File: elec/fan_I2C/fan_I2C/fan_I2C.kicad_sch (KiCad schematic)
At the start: 22 parts, among them J101 DB25_Female_MountingHoles, J102 DB9_Female_MountingHoles, J103 Screw_Terminal_01x02, J104 Conn_01x04, J105 Conn_01x05, J106 Conn_01x04, J107 Conn_01x07, J108 Screw_Terminal_01x02, J109 Conn_02x12_Odd_Even, SW101 SW_DIP_x08

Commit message: Add 3D model to Arduino.
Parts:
- XA101: footprint arduino-library:Arduino_Due_Shield -> PubInv_PCB:Arduino_Due_Shield
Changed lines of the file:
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@@
       (effects (font (size 1.524 1.524)))
     )
-    (property "Footprint" "arduino-library:Arduino_Due_Shield" (id 2) (at 194.31 166.37 0)
+    (property "Footprint" "PubInv_PCB:Arduino_Due_Shield" (id 2) (at 194.31 166.37 0)
       (effects (font (size 1.524 1.524)) hide)
     )
@@
     )
     (path "/53a9b8e5-86db-48fa-b451-066c5e8062db"
-      (reference "XA101") (unit 1) (value "Arduino_Due_Shield") (footprint "arduino-library:Arduino_Due_Shield")
-    )
-  )
+      (reference "XA101") (unit 1) (value "Arduino_Due_Shield") (footprint "PubInv_PCB:Arduino_Due_Shield")
+    )
+  )

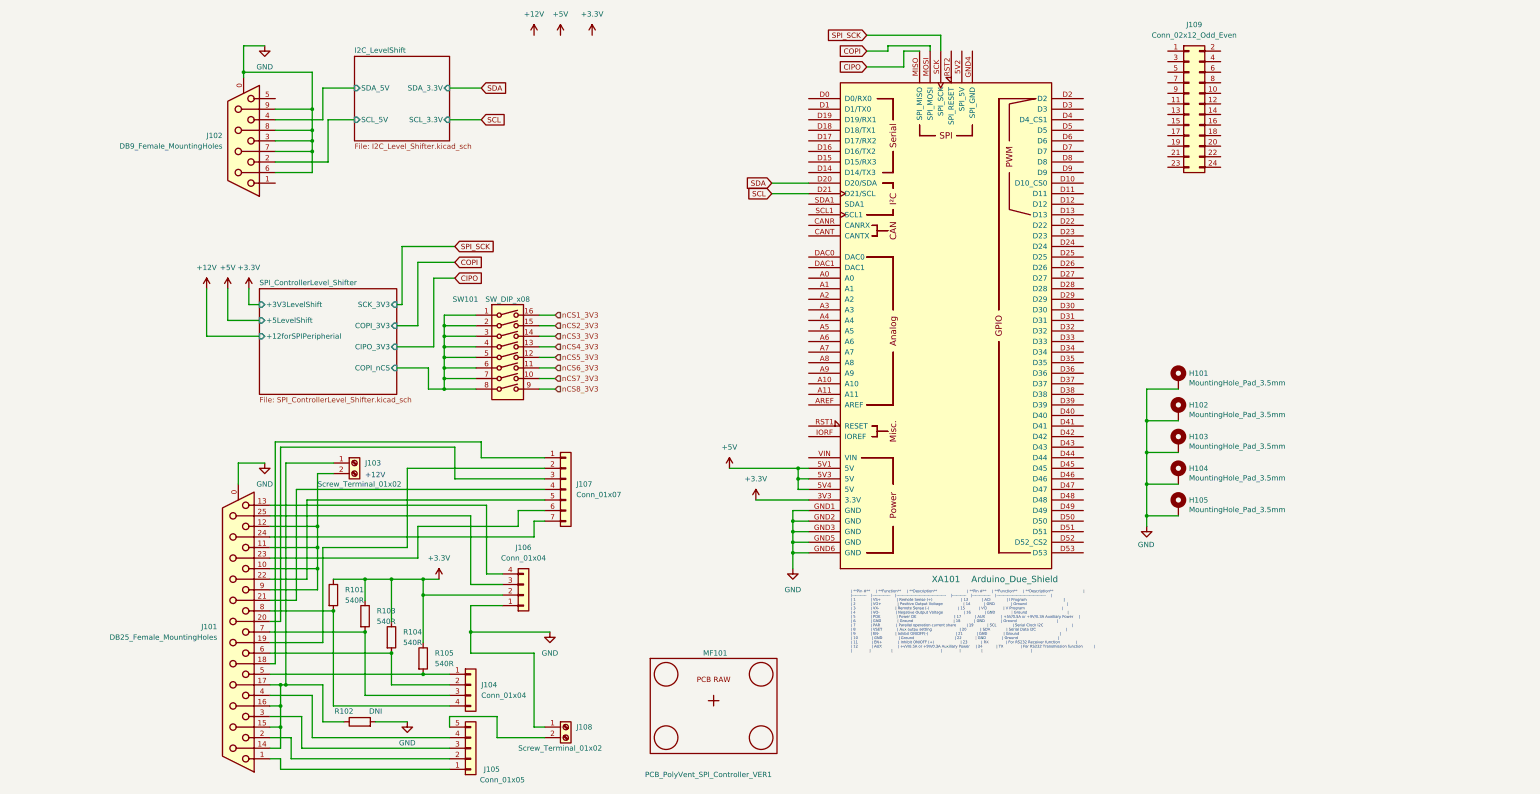
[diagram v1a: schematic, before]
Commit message: Add connectors to pin out the Due.
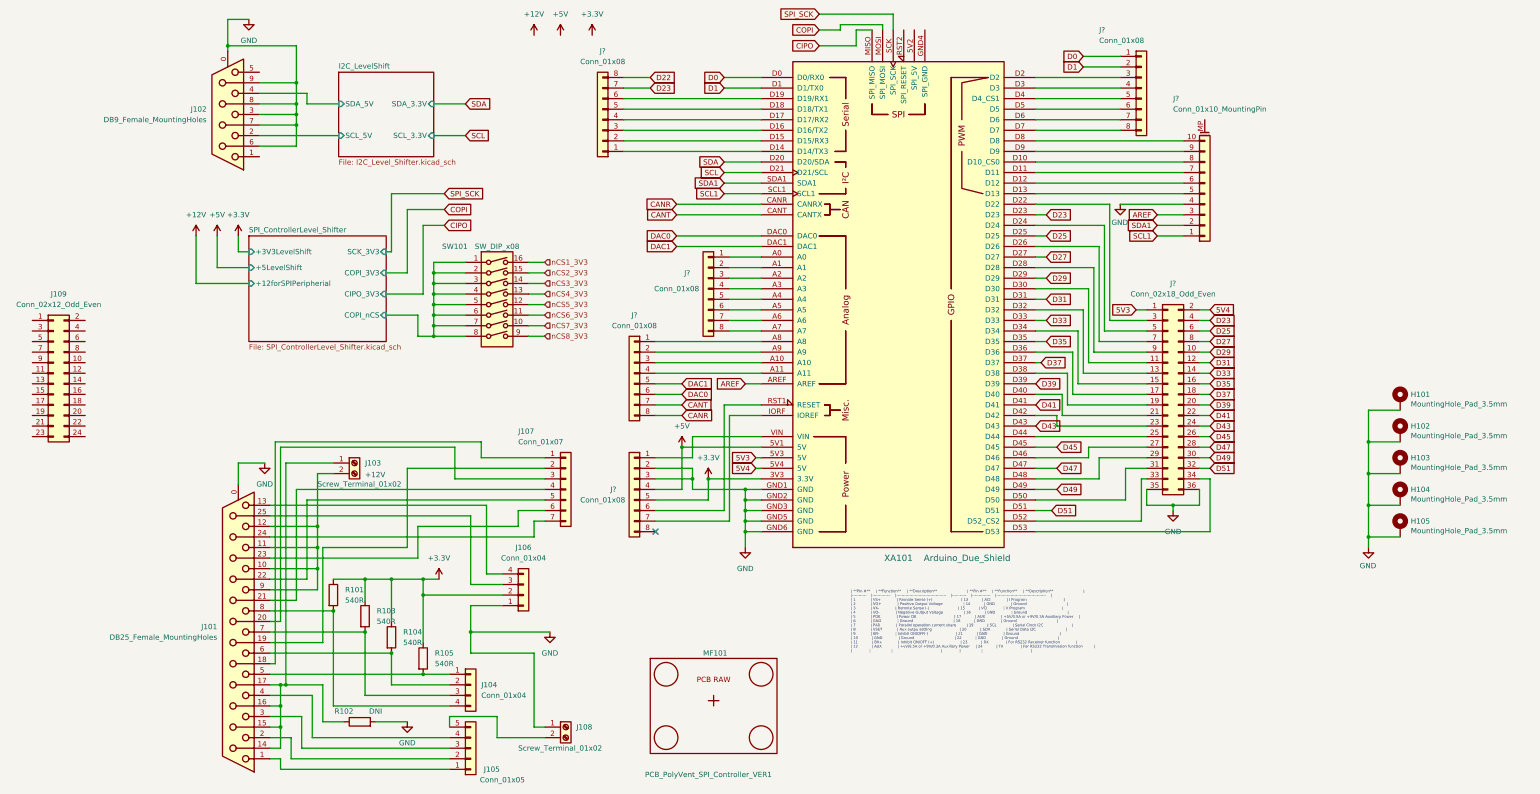
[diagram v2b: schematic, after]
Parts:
- added J? (x5): Conn_01x08, Connector_PinHeader_2.54mm:PinHeader_1x08_P2.54mm_Vertical, symbol Connector_Generic:Conn_01x08
- added J?: Conn_02x18_Odd_Even, symbol Connector_Generic:Conn_02x18_Odd_Even
- added J?: Conn_01x10_MountingPin, Connector_PinHeader_2.54mm:PinHeader_1x10_P2.54mm_Vertical, symbol Connector_Generic_MountingPin:Conn_01x10_MountingPin
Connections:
- net +3.3V: now also J?.5 (Pin_5)
- net +5V: now also J?.4 (Pin_4); no longer XA101.5V3 (5V), XA101.5V4 (5V)
- net GND: now also J?.2 (Pin_2), J?.3 (Pin_3), J?.35 (Pin_35), J?.36 (Pin_36), J?.4 (Pin_4)
- net at XA101.A0: now also J?.1 (Pin_1)
- net at XA101.A1: now also J?.2 (Pin_2)
- net at XA101.A10: now also J?.3 (Pin_3)
- net at XA101.A11: now also J?.4 (Pin_4)
- net at XA101.A2: now also J?.3 (Pin_3)
- net at XA101.A3: now also J?.4 (Pin_4)
- net at XA101.A4: now also J?.5 (Pin_5)
- net at XA101.A5: now also J?.6 (Pin_6)
- net at XA101.A6: now also J?.7 (Pin_7)
- net at XA101.A7: now also J?.8 (Pin_8)
- net at XA101.A8: now also J?.1 (Pin_1)
- net at XA101.A9: now also J?.2 (Pin_2)
- net AREF: now reaches XA101.AREF
- net AREF: now also J?.3 (Pin_3)
- net CANR: now reaches XA101.CANR (CANRX)
- net CANR: now also J?.8 (Pin_8)
- net CANT: now reaches XA101.CANT (CANTX)
- net CANT: now also J?.7 (Pin_7)
- net D0: now reaches XA101.D0 (D0/RX0)
- net D0: now also J?.1 (Pin_1)
- net D1: now reaches XA101.D1 (D1/TX0)
- net D1: now also J?.2 (Pin_2)
- net at XA101.D10 (D10_CS0): now also J?.8 (Pin_8)
- net at XA101.D11: now also J?.7 (Pin_7)
- net at XA101.D12: now also J?.6 (Pin_6)
- net at XA101.D13: now also J?.5 (Pin_5)
- net at XA101.D14 (D14/TX3): now also J?.1 (Pin_1)
- net at XA101.D15 (D15/RX3): now also J?.2 (Pin_2)
- net at XA101.D16 (D16/TX2): now also J?.3 (Pin_3)
- net at XA101.D17 (D17/RX2): now also J?.4 (Pin_4)
- net at XA101.D18 (D18/TX1): now also J?.5 (Pin_5)
- net at XA101.D19 (D19/RX1): now also J?.6 (Pin_6)
- net at XA101.D2: now also J?.3 (Pin_3)
- net at XA101.D22: now also J?.3 (Pin_3)
- net D23: now reaches XA101.D23
- net D23: now also J?.4 (Pin_4), J?.7 (Pin_7)
- net at XA101.D24: now also J?.5 (Pin_5)
- net D25: now reaches XA101.D25
- net D25: now also J?.6 (Pin_6)
- net at XA101.D26: now also J?.7 (Pin_7)
- net D27: now reaches XA101.D27
- net D27: now also J?.8 (Pin_8)
- net at XA101.D28: now also J?.9 (Pin_9)
- net D29: now reaches XA101.D29
- net D29: now also J?.10 (Pin_10)
- net at XA101.D3: now also J?.4 (Pin_4)
- net at XA101.D30: now also J?.11 (Pin_11)
- net D31: now reaches XA101.D31
- net D31: now also J?.12 (Pin_12)
- net at XA101.D32: now also J?.13 (Pin_13)
- net D33: now reaches XA101.D33
- net D33: now also J?.14 (Pin_14)
- net at XA101.D34: now also J?.15 (Pin_15)
- net D35: now reaches XA101.D35
- net D35: now also J?.16 (Pin_16)
- net at XA101.D36: now also J?.17 (Pin_17)
- net D37: now reaches XA101.D37
- net D37: now also J?.18 (Pin_18)
- net at XA101.D38: now also J?.19 (Pin_19)
- net D39: now reaches XA101.D39
- net D39: now also J?.20 (Pin_20)
- net at XA101.D4 (D4_CS1): now also J?.5 (Pin_5)
- net at XA101.D40: now also J?.21 (Pin_21)
- net D41: now reaches XA101.D41
- net D41: now also J?.22 (Pin_22)
- net at XA101.D42: now also J?.23 (Pin_23)
- net D43: now reaches XA101.D43
- net D43: now also J?.24 (Pin_24)
- net at XA101.D44: now also J?.25 (Pin_25)
- net D45: now reaches XA101.D45
- net D45: now also J?.26 (Pin_26)
- net at XA101.D46: now also J?.27 (Pin_27)
- net D47: now reaches XA101.D47
- net D47: now also J?.28 (Pin_28)
- net at XA101.D48: now also J?.29 (Pin_29)
- net D49: now reaches XA101.D49
- net D49: now also J?.30 (Pin_30)
- net at XA101.D5: now also J?.6 (Pin_6)
- net at XA101.D50: now also J?.31 (Pin_31)
- net D51: now reaches XA101.D51
- net D51: now also J?.32 (Pin_32)
- net at XA101.D52 (D52_CS2): now also J?.33 (Pin_33)
- net at XA101.D53: now also J?.34 (Pin_34)
- net at XA101.D6: now also J?.7 (Pin_7)
- net at XA101.D7: now also J?.8 (Pin_8)
- net at XA101.D8: now also J?.10 (Pin_10)
- net at XA101.D9: now also J?.9 (Pin_9)
- net DAC0: now reaches XA101.DAC0
- net DAC0: now also J?.6 (Pin_6)
- net DAC1: now reaches XA101.DAC1
- net DAC1: now also J?.5 (Pin_5)
- net at XA101.IORF (IOREF): now also J?.7 (Pin_7)
- net at XA101.RST1 (RESET): now also J?.6 (Pin_6)
- net SCL1: now reaches XA101.SCL1
- net SCL1: now also J?.1 (Pin_1)
- net SDA1: now reaches XA101.SDA1
- net SDA1: now also J?.2 (Pin_2)
- net at XA101.VIN: now also J?.1 (Pin_1)
- new net 5V3: J?.1 (Pin_1), XA101.5V3 (5V)
- new net 5V4: J?.2 (Pin_2), XA101.5V4 (5V)
- new net D22: J?.8 (Pin_8)
- no-connect marks 0 -> 1
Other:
- moved on the sheet: H101, H102, H103, H104, H105, J102, J109, SW101, XA101

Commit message: Change connector foot prints to sockets.
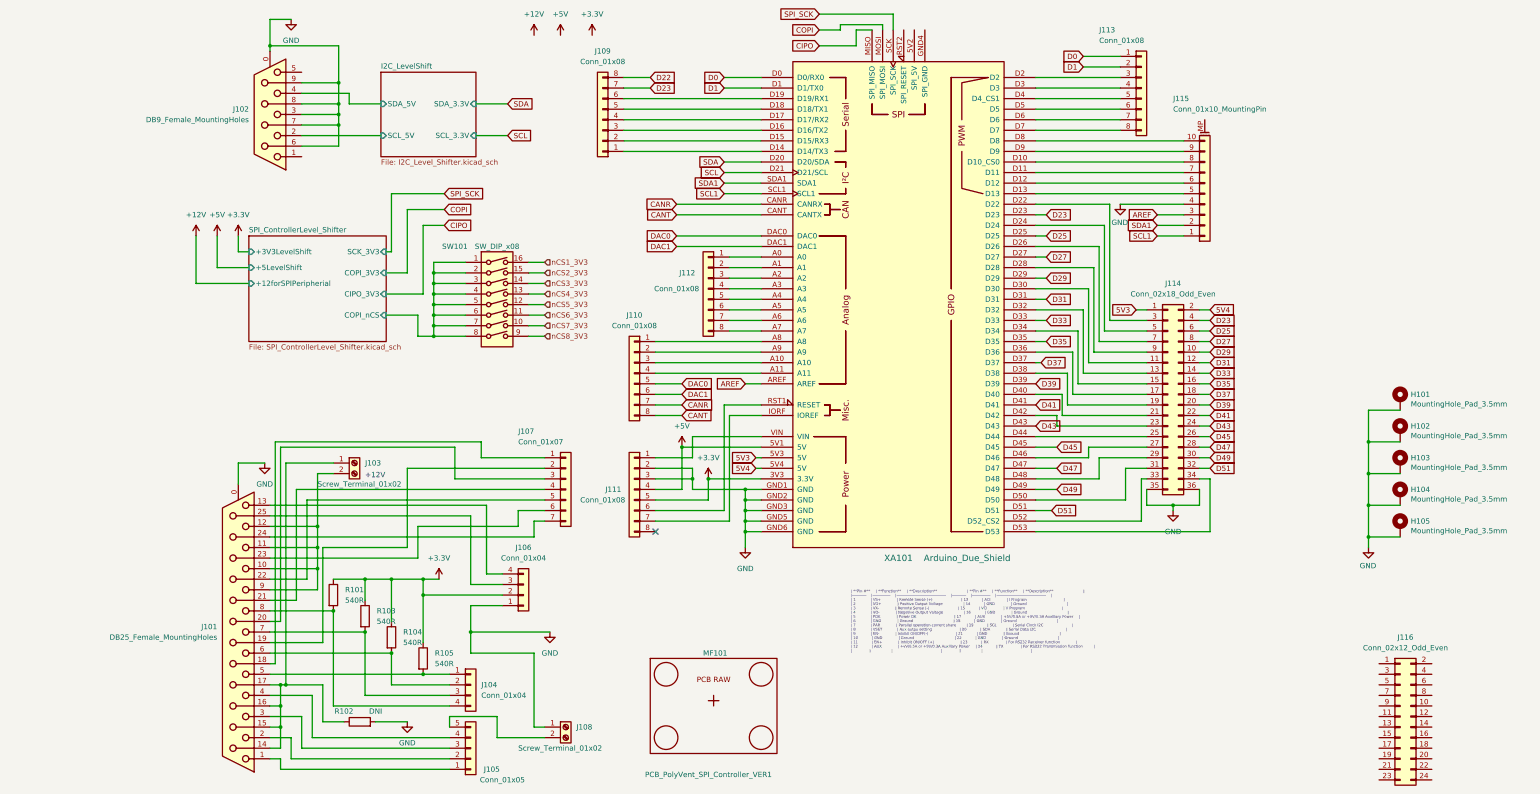
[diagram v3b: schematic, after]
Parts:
- J109, J110, J112, J113: renamed from J?; footprint Connector_PinHeader_2.54mm:PinHeader_1x08_P2.54mm_Vertical -> Connector_PinSocket_2.54mm:PinSocket_1x08_P2.54mm_Vertical
- J114: renamed from J?; footprint (none) -> Connector_PinSocket_2.54mm:PinSocket_2x18_P2.54mm_Vertical
- J115: renamed from J?; footprint Connector_PinHeader_2.54mm:PinHeader_1x10_P2.54mm_Vertical -> Connector_PinSocket_2.54mm:PinSocket_1x10_P2.54mm_Vertical
- gave numbers to parts that had none: 1
- renumbered J109 to J116
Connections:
- net CANR: now also J110.7 (Pin_7); no longer J110.8 (Pin_8)
- net CANT: now also J110.8 (Pin_8); no longer J110.7 (Pin_7)
- net DAC0: now also J110.5 (Pin_5); no longer J110.6 (Pin_6)
- net DAC1: now also J110.6 (Pin_6); no longer J110.5 (Pin_5)
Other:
- moved on the sheet: J102, J116
